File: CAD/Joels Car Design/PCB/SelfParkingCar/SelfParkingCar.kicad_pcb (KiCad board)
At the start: 2 copper layers, 80 x 157.5 mm, 13 parts, among them U1 ESP32-DevKitC

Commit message: PCB Complete
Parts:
- added Cam2: ESP32-CAM, SelfParkingCar:ESP32-CAM, F.Cu at (99.1, 45.3)
- added Cam3: ~, SelfParkingCar:ESP32 Camera, F.Cu at (130.8, 45.3)
- moved Drv1 12.8 mm to (76.7, 92.0)
- moved Bat1 10.6 mm to (76.4, 114.6)
- moved Cam1 5.24 mm to (85.2, 124.4)
- moved Rng5 5.10 mm to (94.8, 25.0)
- moved Rng1 5.09 mm to (95.5, 135.1)
- moved Vreg1 5.09 mm to (87.5, 74.4)
- moved Vreg2 5.09 mm to (87.5, 98.3)
- moved Rng2 5.08 mm to (62.0, 173.5)
- moved Rng4 5.08 mm to (29.2, 25.0)
- moved Rng3 5.07 mm to (28.5, 135.1)
- moved Mot1 1.67 mm to (76.5, 106.6)
- moved Ser1 1.48 mm to (75.2, 110.6)
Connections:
- net +7.5V renamed Batt
- net Net-(Rng3-DOUT) renamed RNG3
- net VCC renamed Mot
- Cam1 pad 1: +5V -> Sen
- Drv1 pad 2: +5V -> +3.3V
- Drv1 pad 3: Net-(Drv1-BIN2(ENABLE)) -> BIN2
- Drv1 pad 4: Net-(Drv1-BIN1(PHASE)) -> BIN1
- Drv1 pad 7: +5V -> +3.3V
- Rng1 pad 3: Net-(Rng1-DOUT) -> RNG1
- Rng2 pad 3: Net-(Rng2-DOUT) -> RNG2
- Rng4 pad 3: Net-(Rng4-DOUT) -> RNG4
- Rng5 pad 3: Net-(Rng5-DOUT) -> RNG5
- Ser1 pad 2: Net-(Ser1-DIN) -> SER1
- U1 pad 19: +5V -> Sen
- U1 pad 25: Net-(Ser1-DIN) -> unconnected-(U1-GPIO0/BOOT/ADC2_CH1-Pad25)
- U1 pad 26: Net-(Rng5-DOUT) -> RNG1
- U1 pad 27: Net-(Rng4-DOUT) -> RNG2
- U1 pad 30: Net-(Rng1-DOUT) -> BIN1
- U1 pad 31: Net-(Rng2-DOUT) -> BIN2
- U1 pad 7: Net-(Drv1-BIN1(PHASE)) -> RNG4
- U1 pad 8: Net-(Drv1-BIN2(ENABLE)) -> RNG5
- Vreg1 pad 1: +5V -> unconnected-(Vreg1-EN-Pad1)
- Vreg1 pad 5: +5V -> Sen
- Vreg2 pad 1: +5V -> unconnected-(Vreg2-EN-Pad1)
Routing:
- net GND: track 399.1 -> 0.00 mm, vias 2 -> 0
- net Sen: track 0.00 -> 223.7 mm
- net +3.3V: track 310.6 -> 464.5 mm, vias 4 -> 0
- net +5V: track 149.2 -> 0.00 mm
- net Net-(Rng5-DOUT): track 139.8 -> 0.00 mm, vias 1 -> 0
- net RNG5: track 0.00 -> 119.4 mm
- net Net-(Rng4-DOUT): track 102.3 -> 0.00 mm, vias 2 -> 0
- net RNG4: track 0.00 -> 94.6 mm
- net Net-(Rng2-DOUT): track 77.4 -> 0.00 mm
- net Net-(Rng1-DOUT): track 75.9 -> 0.00 mm, vias 1 -> 0
- net RNG2: track 0.00 -> 68.7 mm
- net Net-(Drv1-BIN1(PHASE)): track 57.6 -> 0.00 mm
- net RNG1: track 0.00 -> 55.1 mm
- net Net-(Drv1-BIN2(ENABLE)): track 52.5 -> 0.00 mm
- net BIN1: track 0.00 -> 27.1 mm
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- added copper zone on F.Cu, net CAM5V
- added copper zone on B.Cu, net CAMGND
- added copper zone on B.Cu, net GND
- added copper zone on F.Cu, net GND
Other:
- board size 80 x 157.5 mm -> 110.1 x 158.2 mm

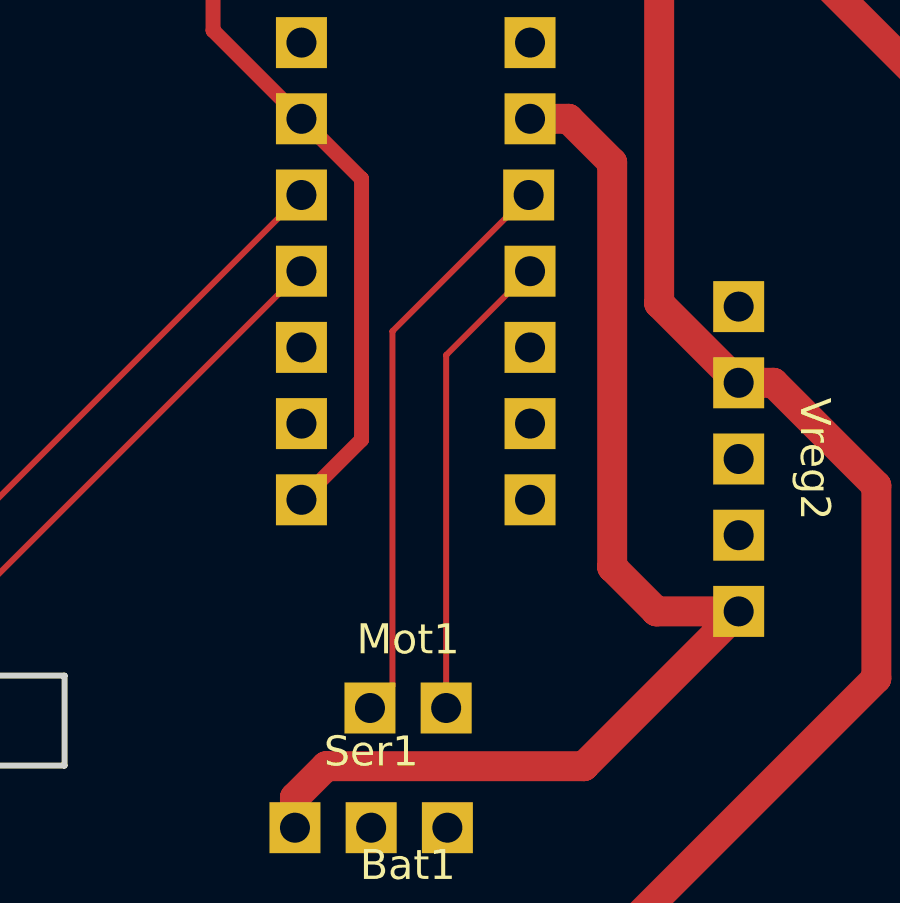
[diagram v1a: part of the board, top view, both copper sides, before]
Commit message: Code for camera working (unreliable)
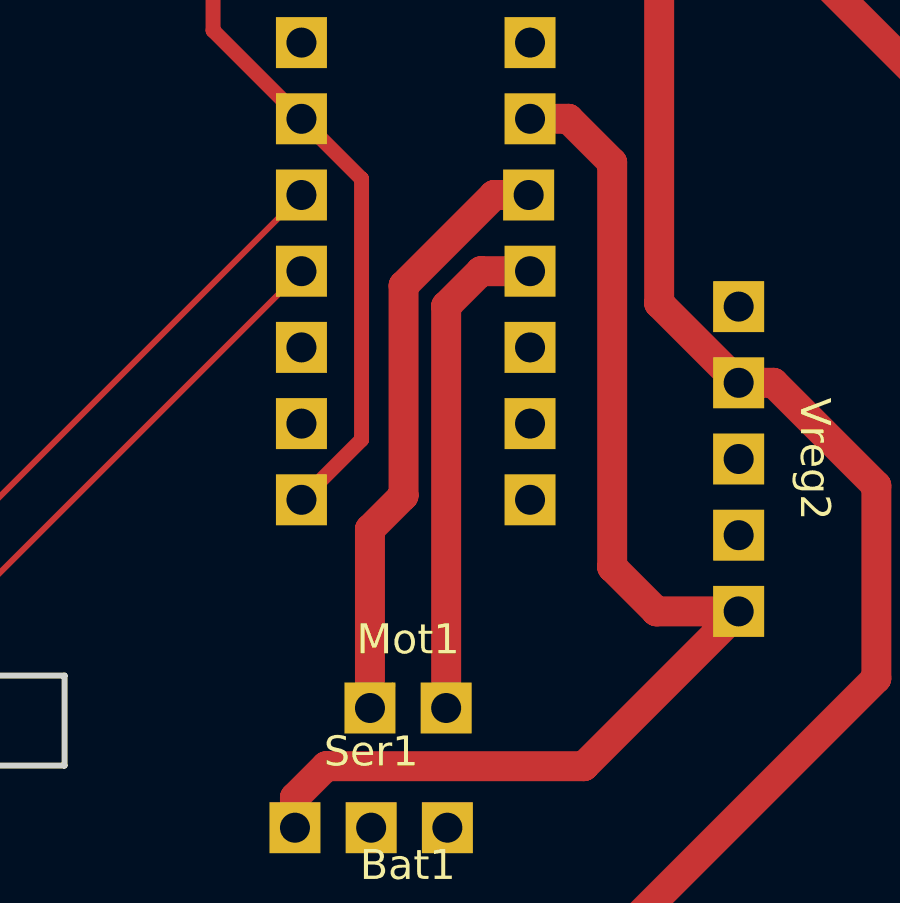
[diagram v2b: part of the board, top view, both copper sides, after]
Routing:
- net Net-(Drv1-BOUT2): track 19.3 -> 21.0 mm
- net Net-(Drv1-BOUT1): track 15.7 -> 16.7 mm
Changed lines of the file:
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@@
 	)
 	(segment
-		(start 75.93 94.020009)
-		(end 75.93 105.83)
-		(width 0.2)
+		(start 80.470009 89.48)
+		(end 79.32 89.48)
+		(width 1)
+		(layer "F.Cu")
+		(net 33)
+	)
+	(segment
+		(start 75.18 100.62)
+		(end 75.18 106.58)
+		(width 1)
+		(layer "F.Cu")
+		(net 33)
+	)
+	(segment
+		(start 76.3 92.5)
+		(end 76.3 99.5)
+		(width 1)
+		(layer "F.Cu")
+		(net 33)
+	)
+	(segment
+		(start 76.3 99.5)
+		(end 75.18 100.62)
+		(width 1)
+		(layer "F.Cu")
+		(net 33)
+	)
+	(segment
+		(start 79.32 89.48)
+		(end 76.3 92.5)
+		(width 1)
 		(layer "F.Cu")
 		(net 33)
@@
 		(start 75.93 105.83)
 		(end 75.18 106.58)
-		(width 0.2)
-		(layer "F.Cu")
-		(net 33)
-	)
-	(segment
-		(start 80.470009 89.48)
-		(end 75.93 94.020009)
 		(width 0.2)
 		(layer "F.Cu")
@@
 	)
 	(segment
-		(start 77.72 106.58)
-		(end 77.72 94.816)
-		(width 0.2)
+		(start 78.88 92.02)
+		(end 80.516 92.02)
+		(width 1)
 		(layer "F.Cu")
 		(net 35)
 	)
 	(segment
-		(start 77.72 94.816)
-		(end 80.516 92.02)
-		(width 0.2)
+		(start 77.72 93.18)
+		(end 78.88 92.02)
+		(width 1)
 		(layer "F.Cu")
 		(net 35)
+	)
+	(segment
+		(start 77.72 106.58)
+		(end 77.72 93.18)
+		(width 1)
+		(layer "F.Cu")
+		(net 35)

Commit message: PCB Joel's Final Design
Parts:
- moved Cam3 0.19 mm to (130.6, 45.3)
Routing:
- net +3.3V: track 464.5 -> 471.8 mm
- net RNG4: track 94.6 -> 95.8 mm
- net Batt: track 61.5 -> 62.3 mm
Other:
- outline, holes or cut-outs redrawn
